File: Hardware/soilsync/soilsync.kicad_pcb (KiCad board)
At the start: 2 copper layers, 21 parts, among them J1 Barrel_Jack_Switch, J10 Screw_Terminal_01x03, J11 Screw_Terminal_01x03, J12 Screw_Terminal_01x03, J13 Conn_Battery, J2 Screw_Terminal_01x03, J3 Screw_Terminal_01x03, J4 Screw_Terminal_01x03, J5 Screw_Terminal_01x03, J6 Screw_Terminal_01x03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

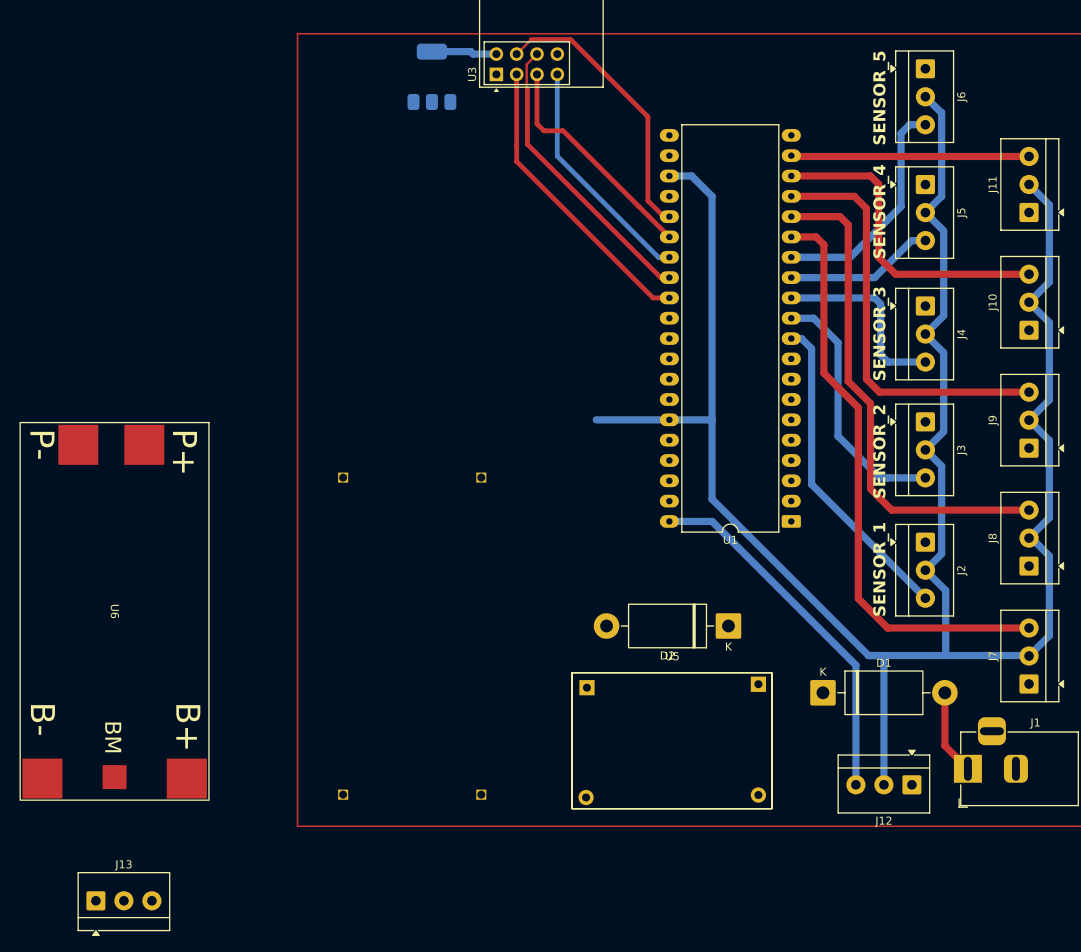
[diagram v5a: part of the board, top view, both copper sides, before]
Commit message: layout nearly finished.
need to add mosfet and programming connector
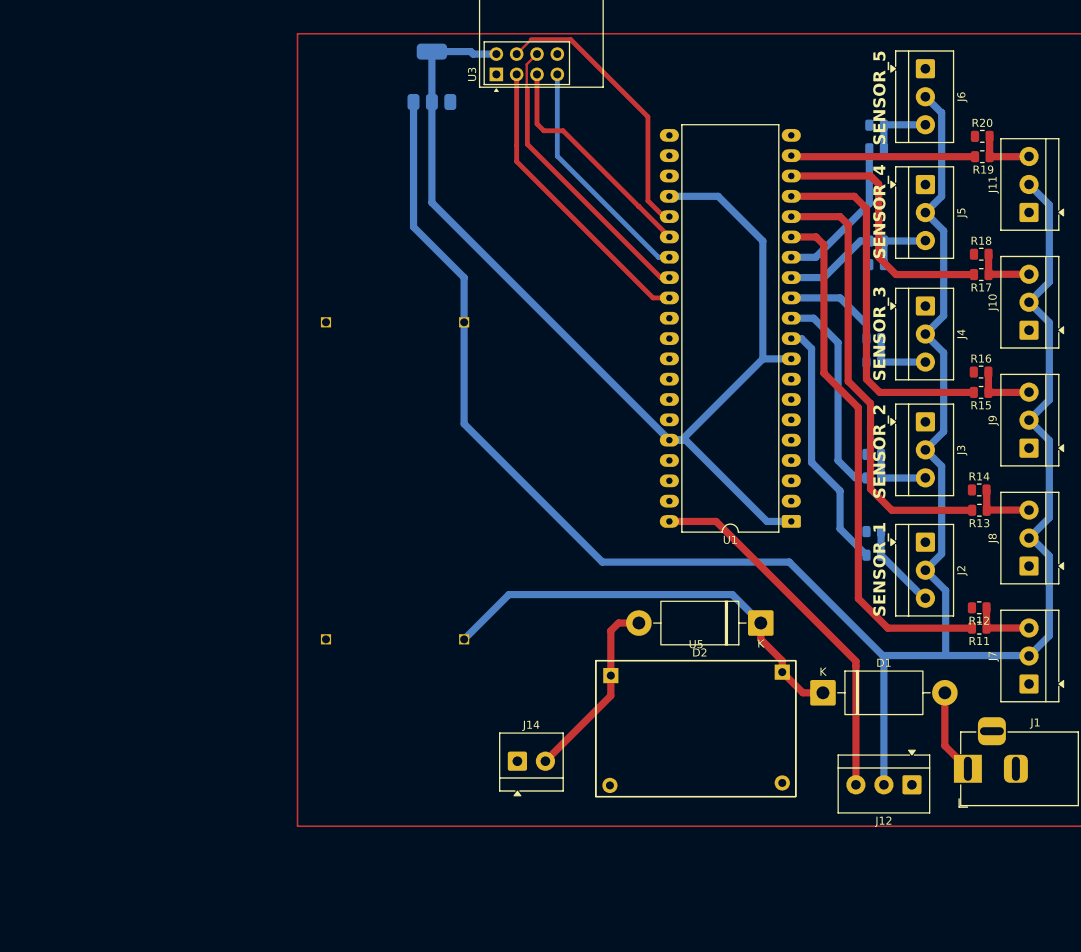
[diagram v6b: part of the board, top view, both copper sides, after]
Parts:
- removed J13: Conn_Battery, TerminalBlock_4Ucon:TerminalBlock_4Ucon_1x03_P3.50mm_Horizontal
- removed U6: HX-2S, CustomModule:HX-2S BMS module
- added J14: BMS_Terminal, TerminalBlock_4Ucon:TerminalBlock_4Ucon_1x02_P3.50mm_Horizontal, F.Cu at (192.6, 117.6)
- added R1: 4.7k, Resistor_SMD:R_0805_2012Metric, B.Cu at (237.1, 91.8)
- added R10: 8.2k, Resistor_SMD:R_0805_2012Metric, B.Cu at (237.5, 38.1)
- added R11: 4.7k, Resistor_SMD:R_0805_2012Metric, F.Cu at (250.3, 101.0)
- added R12: 8.2k, Resistor_SMD:R_0805_2012Metric, F.Cu at (250.3, 98.4)
- added R13: 4.7k, Resistor_SMD:R_0805_2012Metric, F.Cu at (250.3, 86.2)
- added R14: 8.2k, Resistor_SMD:R_0805_2012Metric, F.Cu at (250.3, 83.7)
- added R15: 4.7k, Resistor_SMD:R_0805_2012Metric, F.Cu at (250.5, 71.5)
- added R16: 8.2k, Resistor_SMD:R_0805_2012Metric, F.Cu at (250.5, 69.0)
- added R17: 4.7k, Resistor_SMD:R_0805_2012Metric, F.Cu at (250.6, 56.8)
- added R18: 8.2k, Resistor_SMD:R_0805_2012Metric, F.Cu at (250.6, 54.2)
- added R19: 4.7k, Resistor_SMD:R_0805_2012Metric, F.Cu at (250.7, 42.0)
- added R2: 8.2k, Resistor_SMD:R_0805_2012Metric, B.Cu at (237.1, 88.9)
- added R20: 8.2k, Resistor_SMD:R_0805_2012Metric, F.Cu at (250.7, 39.5)
- added R3: 4.7k, Resistor_SMD:R_0805_2012Metric, B.Cu at (237.1, 82.2)
- added R4: 8.2k, Resistor_SMD:R_0805_2012Metric, B.Cu at (237.1, 79.2)
- added R5: 4.7k, Resistor_SMD:R_0805_2012Metric, B.Cu at (237.1, 64.8)
- added R6: 8.2k, Resistor_SMD:R_0805_2012Metric, B.Cu at (237.1, 67.7)
- added R7: 4.7k, Resistor_SMD:R_0805_2012Metric, B.Cu at (237.5, 52.6)
- added R8: 8.2k, Resistor_SMD:R_0805_2012Metric, B.Cu at (237.5, 55.5)
- added R9: 4.7k, Resistor_SMD:R_0805_2012Metric, B.Cu at (237.5, 41.0)
- moved U2 19.5 mm to (187.7, 104.5)
- moved D2 4.06 mm to (223.0, 100.3)
- moved U5 3.35 mm to (214.9, 113.5)
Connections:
- J10 pad 3: SENSOR_9 -> Net-(J10-Pin_3)
- J11 pad 3: SENSOR_10 -> Net-(J11-Pin_3)
- J2 pad 3: SENSOR_1 -> Net-(J2-Pin_3)
- J3 pad 3: SENSOR_2 -> Net-(J3-Pin_3)
- J4 pad 3: SENSOR_3 -> Net-(J4-Pin_3)
- J5 pad 3: SENSOR_4 -> Net-(J5-Pin_3)
- J6 pad 3: SENSOR_5 -> Net-(J6-Pin_3)
- J7 pad 3: SENSOR_6 -> Net-(J7-Pin_3)
- J8 pad 3: SENSOR_7 -> Net-(J8-Pin_3)
- J9 pad 3: SENSOR_8 -> Net-(J9-Pin_3)
- U1 pad 1: unconnected-(U1-VBAT-Pad1) -> +3.3V
- U1 pad 23: +5V -> GND
- U1 pad 24: unconnected-(U1-VDD-Pad24) -> +3.3V
- U1 pad 35: +5V -> GND
- U1 pad 36: unconnected-(U1-VDD-Pad36) -> +3.3V
- U1 pad 8: unconnected-(U1-VSSA-Pad8) -> GND
- U1 pad 9: unconnected-(U1-VDDA-Pad9) -> +3.3V
- U5 pad 2: /BAT- -> GND
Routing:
- net +3.3V: track 8.18 -> 136.7 mm
- net VIN: track 0.00 -> 54.3 mm
- net /BAT+: track 0.00 -> 23.6 mm
- net +5V: track 270.1 -> 287.3 mm
- net SENSOR_3: track 23.8 -> 12.5 mm
- net Net-(J2-Pin_3): track 0.00 -> 10.7 mm
- net SENSOR_5: track 29.0 -> 19.4 mm
- net Net-(J4-Pin_3): track 0.00 -> 8.50 mm
- net Net-(J3-Pin_3): track 0.00 -> 8.50 mm
- net SENSOR_1: track 40.1 -> 31.7 mm
- net Net-(J6-Pin_3): track 0.00 -> 8.16 mm
- net Net-(J5-Pin_3): track 0.00 -> 8.16 mm
- net Net-(J7-Pin_3): track 0.00 -> 7.86 mm
- net Net-(J8-Pin_3): track 0.00 -> 7.85 mm
- net Net-(J9-Pin_3): track 0.00 -> 7.63 mm
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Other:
- board text removed: "${REFERENCE}"

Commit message: PCB Finished
Generated fabrication data
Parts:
- added D4: MBRS340, Diode_SMD:D_SMC, F.Cu at (183.9, 47.4)
- added Q1: IRLZ44N, Package_TO_SOT_THT:TO-220-3_Vertical, B.Cu at (192.5, 44.5)
- added R22: 100, Resistor_SMD:R_1206_3216Metric_Pad1.30x1.75mm_HandSolder, F.Cu at (205.7, 47.5)
- D1: value MBR340 -> MBRS340; footprint Diode_THT:D_DO-201AD_P15.24mm_Horizontal -> Diode_SMD:D_SMC
- D2: value MBR340 -> MBRS340; footprint Diode_THT:D_DO-201AD_P15.24mm_Horizontal -> Diode_SMD:D_SMC; moved to B.Cu
- J12: value Screw_Terminal_01x03 -> PUMP_Terminal; footprint TerminalBlock_4Ucon:TerminalBlock_4Ucon_1x03_P3.50mm_Horizontal -> TerminalBlock_4Ucon:TerminalBlock_4Ucon_1x02_P3.50mm_Horizontal
- R1, R10, R2, R3, R4, R5, R6, R7, R8, R9: moved to F.Cu
- R11, R12, R13, R14, R15, R16, R17, R18, R19, R20: moved to B.Cu
- U1: value STM32F103C8Tx -> YAAJ_BluePill; moved to B.Cu
- moved J12 101.1 mm to (173.9, 45.7), turned to -90 degrees
- moved J2 59.2 mm to (243.6, 31.0)
- moved J6 59.2 mm to (243.6, 90.2)
- moved J11 58.9 mm to (256.5, 108.0)
- moved J7 58.9 mm to (256.5, 49.0)
- moved R11 58.9 mm to (250.7, 42.0)
- moved R19 58.9 mm to (250.3, 101.0)
- moved R12 58.9 mm to (250.7, 39.5)
- moved R20 57.7 mm to (250.3, 97.2)
- moved R10 53.8 mm to (237.5, 91.8)
- moved R2 50.8 mm to (237.1, 38.1)
- moved R1 50.8 mm to (237.1, 41.0)
- moved R9 47.9 mm to (237.5, 88.9)
- moved U3 43.4 mm to (200.2, 74.0), turned to 180 degrees
- moved R3 33.2 mm to (237.1, 49.0)
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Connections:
- J12 pad 1: GND -> +5V
- J12 pad 2: +5V -> /PUMP-
- U1 pad 1: +3.3V -> /NRF_CSN
- U1 pad 10: SENSOR_1 -> unconnected-(U1-PA15-Pad10)
- U1 pad 11: SENSOR_2 -> unconnected-(U1-PB3-Pad11)
- U1 pad 12: SENSOR_3 -> /PUMP
- U1 pad 13: SENSOR_4 -> unconnected-(U1-PB5-Pad13)
- U1 pad 14: SENSOR_5 -> unconnected-(U1-PB6-Pad14)
- U1 pad 15: SENSOR_6 -> unconnected-(U1-PB7-Pad15)
- U1 pad 16: SENSOR_7 -> unconnected-(U1-PB8-Pad16)
- U1 pad 17: SENSOR_8 -> unconnected-(U1-PB9-Pad17)
- U1 pad 18: SENSOR_9 -> unconnected-(U1-5V-Pad18)
- U1 pad 19: SENSOR_10 -> GND
- U1 pad 2: unconnected-(U1-PC13-Pad2) -> /NRF_SCK
- U1 pad 20: unconnected-(U1-PB2-Pad20) -> +3.3V
- U1 pad 23: GND -> unconnected-(U1-PC14-Pad23)
- U1 pad 24: +3.3V -> unconnected-(U1-PC15-Pad24)
- U1 pad 25: /NRF_CSN -> SENSOR_1
- U1 pad 26: /NRF_SCK -> SENSOR_2
- U1 pad 27: /NRF_MISO -> SENSOR_3
- U1 pad 28: /NRF_MOSI -> SENSOR_4
- U1 pad 29: /NRF_CE -> SENSOR_5
- U1 pad 3: unconnected-(U1-PC14-Pad3) -> /NRF_MISO
- U1 pad 30: unconnected-(U1-PA9-Pad30) -> SENSOR_6
- U1 pad 31: unconnected-(U1-PA10-Pad31) -> SENSOR_7
- U1 pad 32: unconnected-(U1-PA11-Pad32) -> SENSOR_8
- U1 pad 33: unconnected-(U1-PA12-Pad33) -> SENSOR_9
- U1 pad 34: unconnected-(U1-PA13-Pad34) -> SENSOR_10
- U1 pad 35: GND -> unconnected-(U1-PB10-Pad35)
- U1 pad 36: +3.3V -> unconnected-(U1-PB11-Pad36)
- U1 pad 38: unconnected-(U1-PA15-Pad38) -> +3.3V
- U1 pad 39: unconnected-(U1-PB3-Pad39) -> GND
- U1 pad 4: unconnected-(U1-PC15-Pad4) -> /NRF_MOSI
- U1 pad 40: PUMP -> GND
- U1 pad 5: unconnected-(U1-PD0-Pad5) -> /NRF_CE
- U1 pad 8: GND -> unconnected-(U1-PA11-Pad8)
- U1 pad 9: +3.3V -> unconnected-(U1-PA12-Pad9)
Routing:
- net PUMP: track 46.0 -> 0.00 mm
- net +3.3V: track 136.7 -> 100.2 mm
- net SENSOR_6: track 66.2 -> 37.8 mm
- net SENSOR_7: track 55.5 -> 27.9 mm
- net SENSOR_10: track 23.2 -> 47.0 mm
- net /NRF_CE: track 37.0 -> 13.6 mm
- net /PUMP-: track 0.00 -> 20.8 mm
- net SENSOR_8: track 45.5 -> 25.1 mm
- net SENSOR_4: track 11.6 -> 29.8 mm
- net SENSOR_1: track 31.7 -> 13.7 mm
- net SENSOR_5: track 19.4 -> 36.3 mm
- net SENSOR_2: track 26.3 -> 10.9 mm
- net /PUMP: track 0.00 -> 14.7 mm
- net VIN: track 54.3 -> 68.2 mm
- net Net-(Q1-G): track 0.00 -> 13.9 mm
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- added copper zone on B.Cu, net GND
- added copper zone on F.Cu, net GND
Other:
- board outline added: 96.9 x 97.3 mm
- board text added: "BMS"
- board text added: "PUMP"

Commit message: added Servo pin headers
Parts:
- added J15: USART, Connector_PinHeader_2.54mm:PinHeader_1x02_P2.54mm_Vertical, F.Cu at (202.1, 30.1)
- added J16: SERVO, Connector_PinHeader_2.54mm:PinHeader_1x03_P2.54mm_Vertical, F.Cu at (179.8, 30.9)
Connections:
- U1 pad 14: unconnected-(U1-PB6-Pad14) -> /PWM
- U1 pad 6: unconnected-(U1-PA9-Pad6) -> /USART_TX
- U1 pad 7: unconnected-(U1-PA10-Pad7) -> /USART_RX
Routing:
- net /USART_TX: track 0.00 -> 56.3 mm
- net /USART_RX: track 0.00 -> 53.5 mm
- net /PWM: track 0.00 -> 43.4 mm, vias 0 -> 2
- net +5V: track 294.4 -> 306.1 mm
- net /NRF_MISO: track 30.7 -> 26.6 mm
- net /NRF_MOSI: track 25.7 -> 22.8 mm
- net /NRF_CE: track 13.6 -> 14.4 mm
- net GND: vias 246 -> 647
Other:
- board text added: "LM2596"
- board text added: "NRF24L01"
- board text added: "SERVO"
- board text added: "TP5100"
- board text added: "U2"
- board text added: "USART"
